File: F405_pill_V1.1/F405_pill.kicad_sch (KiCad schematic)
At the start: 42 parts, among them J1 Conn_01x04_Male, J2 Conn_01x04_Male, J4 TYPE-C-31-M-12, U1 STM32F405RGTx, U2 TCAN1051HDR, U3 LM1117-3.3, U4 STM32F405_pill, Y1 Crystal_GND24

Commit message: generated gerbers / BOMs
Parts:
- C3, C6: value 18p -> 12p; LCSC C92671 -> C1642
- D3: LCSC C87326 -> C90692
- R9: value 10k -> 20k; LCSC C269701 -> C365403
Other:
- note added: "Changes: power LED power LED resistor 18pF caps --> 12pF on xtal."
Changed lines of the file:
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@@
+    (effects (font (size 1.27 1.27)) (justify left bottom))
+  )
+  (text "Changes: \npower LED \npower LED resistor\n18pF caps --> 12pF on xtal."
+    (at 181.864 176.53 0)
     (effects (font (size 1.27 1.27)) (justify left bottom))
   )
@@
       (effects (font (size 1.27 1.27)) (justify left))
     )
-    (property "Value" "18p" (id 1) (at 46.99 74.9362 0)
+    (property "Value" "12p" (id 1) (at 46.99 74.9362 0)
       (effects (font (size 1.27 1.27)) (justify left))
     )
@@
       (effects (font (size 1.27 1.27)) hide)
     )
-    (property "LCSC" "C92671" (id 4) (at 44.45 73.66 0)
+    (property "LCSC" "C1642" (id 4) (at 44.45 73.66 0)
       (effects (font (size 1.27 1.27)) hide)
     )
@@
       (effects (font (size 1.27 1.27)) (justify left))
     )
-    (property "Value" "18p" (id 1) (at 24.13 74.93 0)
+    (property "Value" "12p" (id 1) (at 24.13 74.93 0)
       (effects (font (size 1.27 1.27)) (justify left))
     )
@@
       (effects (font (size 1.27 1.27)) hide)
     )
-    (property "LCSC" "C92671" (id 4) (at 29.845 73.66 0)
+    (property "LCSC" "C1642" (id 4) (at 29.845 73.66 0)
       (effects (font (size 1.27 1.27)) hide)
     )
@@
       (effects (font (size 1.27 1.27)) (justify right))
     )
-    (property "Value" "10k" (id 1) (at 270.51 64.77 0)
+    (property "Value" "20k" (id 1) (at 270.51 64.77 0)
       (effects (font (size 1.27 1.27)) (justify right))
     )
@@
       (effects (font (size 1.27 1.27)) hide)
     )
-    (property "LCSC" "C269701" (id 4) (at 267.97 62.23 0)
+    (property "LCSC" "C365403" (id 4) (at 267.97 62.23 0)
       (effects (font (size 1.27 1.27)) hide)
     )
@@
       (effects (font (size 1.27 1.27)) hide)
     )
-    (property "LCSC" "C87326" (id 6) (at 267.97 52.07 0)
+    (property "LCSC" "C90692" (id 6) (at 267.97 52.07 0)
       (effects (font (size 1.27 1.27)) hide)
     )
@@
     )
     (path "/6e59773b-20cf-43bf-aecf-380aa682d29d"
-      (reference "C3") (unit 1) (value "18p") (footprint "Capacitor_SMD:C_0603_1608Metric")
+      (reference "C3") (unit 1) (value "12p") (footprint "Capacitor_SMD:C_0603_1608Metric")
     )
     (path "/40c82e52-98e4-4cad-a0d7-023fceadffa0"
@@
     )
     (path "/1ec141c7-7133-40d6-b34a-de571f2b6dac"
-      (reference "C6") (unit 1) (value "18p") (footprint "Capacitor_SMD:C_0603_1608Metric")
+      (reference "C6") (unit 1) (value "12p") (footprint "Capacitor_SMD:C_0603_1608Metric")
     )
     (path "/ed8ad173-5f47-4e49-8771-8d0e48ed290e"
@@
     )
     (path "/ae295267-9bf4-4191-9631-7bb1dcc66970"
-      (reference "R9") (unit 1) (value "10k") (footprint "Resistor_SMD:R_0603_1608Metric")
+      (reference "R9") (unit 1) (value "20k") (footprint "Resistor_SMD:R_0603_1608Metric")
     )
     (path "/dba039c0-b01d-4dd9-be13-4d264a7c44db"

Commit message: new work
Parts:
- added C?: ??, Capacitor_SMD:C_0402_1005Metric, symbol Device:C_Small
- added R?: ??, Resistor_SMD:R_0603_1608Metric, symbol Device:R_Small
- added R?: 20k, Resistor_SMD:R_0603_1608Metric, symbol Device:R_Small
- R5: value 5k -> 20k; LCSC C365441 -> C365403
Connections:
- net GND: now also R?.1; no longer U2.5 (VIO)
- net USB_D+: no longer U4.29 (USB_D+)
- net USB_D-: no longer U4.28 (USB_D-)
- net at D2.1 (K), R5.2: no longer D1.1 (K)
- new net: D1.1 (K), R?.2
- new net DUAL1: U4.28 (DUAL1)
- new net DUAL2: U4.29 (DUAL2)
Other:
- note added: "ASSIGN PIN 5, VREF, TO WHAT?"
- note added: "A_OVERLIMIT LIN_A LIB_B LIB_C HIN_A HIN_B HIN_C V5V GND V3V3"
- note added: "Changes: Change caps on xtal from 18pF to 12pF Separate the two LEDs from the single resistor Remove ground from VIO pin on CAN RC between usb shell and pb12 to stop false trips"
- note added: "NC GND NC JP3 A_PHC_VSENSE JP2 A_PHB_VSENSE A_PHA_VSENSE A_SHC_AMP A_SHB_AMP A_SHA_AMP VSENSE A_THROTTLE JP3 HALL_C HALL_B HALL_A NC"
- note removed: "A_OVERLIMIT LIN_A LIB_B LIB_C HIN_A HIN_B HIN_C DUSB_DM DUSB_DP TIM2 CH1 TIM2 CH2 TIM3 CH1 TIM3 CH2 D_UART1_TX I2C1_SCL TIM4_CH1 D_UART1_RX I2C1_SDA TIM4_CH2 DI2C1_SCL TIM4_CH3 DI2C1_SDA TIM4_CH4 V5V GND V3V3"
- note removed: "Changes: power LED power LED resistor 18pF caps --> 12pF on xtal."
- note removed: "Fig 17 https://www.nxp.com/docs/en/supporting-information/AH1014.pdf"
- note removed: "NC GND NC PB10 D_GPIO PB2 D_GPIO JP3 A_PHC_VSENSE JP2 A_PHB_VSENSE A_PHA_VSENSE A_SHC_AMP A_SHB_AMP A_SHA_AMP VSENSE A_THROTTLE JP3 HALL_C HALL_B HALL_A NC"
- note removed: "TCAN1051HDR chip -- cheap at jlcpcb connect pin 3 to 5.0v pin 5 to 3.3v based on page 26 of the TCAN1051 data sheet"
- note removed: "https://easyeda.com/modules/ USB-C-Connector-circuit_245d3825d58f42648e08f3b1c22af371"
- moved on the sheet: C1, C10, C11, C12, C13, C14, C15, C16, C17, C18, C19, C2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

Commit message: new notes
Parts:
- added R12, R8: 1k, Resistor_SMD:R_0402_1005Metric, symbol Device:R_Small
- D3: footprint LED_SMD:LED_0603_1608Metric -> LED_SMD:LED_0402_1005Metric_Pad0.77x0.64mm_HandSolder
- R1, R2: footprint Resistor_SMD:R_0603_1608Metric -> Resistor_SMD:R_0402_1005Metric; LCSC C269701 -> (none)
- R10, R11: footprint Resistor_SMD:R_0603_1608Metric -> Resistor_SMD:R_0402_1005Metric; LCSC C365441 -> (none)
- R3, R4: footprint Resistor_SMD:R_0603_1608Metric -> Resistor_SMD:R_0402_1005Metric; LCSC C101133 -> (none)
- R5, R9: footprint Resistor_SMD:R_0603_1608Metric -> Resistor_SMD:R_0402_1005Metric; LCSC C365403 -> (none)
- R6: renamed from R?; footprint Resistor_SMD:R_0603_1608Metric -> Resistor_SMD:R_0402_1005Metric
- R7: renamed from R?; footprint Resistor_SMD:R_0603_1608Metric -> Resistor_SMD:R_0402_1005Metric; LCSC C365403 -> (none)
- gave numbers to parts that had none: 1
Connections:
- net PC4 is gone; now on net DUAL1: U1.24 (PC4)
- net PC5 is gone; now on net DUAL2: U1.25 (PC5)
- net DUAL1: now also R8.1
- net DUAL2: now also R12.1
- net PA5: now also U4.17 (PA5)
- net PB10: now also R8.2; no longer U4.34 (PB7)
- net PB11: now also R12.2; no longer U4.35 (PC10)
- net PB3: now also U4.30 (PB3); no longer U4.17 (PA5)
- net PB4: now also U4.31 (PB4); no longer U4.33 (PB6)
- net PB6: now also U4.33 (PB6); no longer U4.31 (PB4)
- net PB7: now also U4.34 (PB7); no longer U4.30 (PB3)
- net PB8: no longer U4.36 (PC11)
- net PB9: no longer U4.37 (PC12)
- net PC10: now also U4.35 (PC10)
- net PC11: now also U4.36 (PC11)
- net PC12: now also U4.37 (PC12)
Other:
- moved on the sheet: C17, C18, C19

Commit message: new text
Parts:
- C1: footprint Capacitor_SMD:C_0603_1608Metric -> Capacitor_SMD:C_0402_1005Metric; LCSC C19666 -> (none)
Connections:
- net PA15: now also D2.2 (A)
- net PC10: now also U4.37 (PC12); no longer U4.35 (PC10)
- net PC12: now also U4.35 (PC10); no longer D2.2 (A), U4.37 (PC12)
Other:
- note added: "Changes: Change caps on xtal from 18pF to 12pF Separate the two LEDs from the single resistor Remove ground from VIO pin on CAN RC between usb shell and pb12 to stop false trips PC12->PA15 to drive LED"
- note removed: "Changes: Change caps on xtal from 18pF to 12pF Separate the two LEDs from the single resistor Remove ground from VIO pin on CAN RC between usb shell and pb12 to stop false trips"
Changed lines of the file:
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@@
     (effects (font (size 1.27 1.27)) (justify left bottom))
   )
-  (text "Changes: \nChange caps on xtal from 18pF to 12pF\nSeparate the two LEDs from the single resistor\nRemove ground from VIO pin on CAN\nRC between usb shell and pb12 to stop false trips\n"
+  (text "Changes: \nChange caps on xtal from 18pF to 12pF\nSeparate the two LEDs from the single resistor\nRemove ground from VIO pin on CAN\nRC between usb shell and pb12 to stop false trips\nPC12->PA15 to drive LED\n"
     (at 152.908 167.894 0)
     (effects (font (size 1.27 1.27)) (justify left bottom))
@@
     )
   )
-  (global_label "PC12" (shape input) (at 151.003 71.755 180) (fields_autoplaced)
+  (global_label "PC10" (shape input) (at 151.003 71.755 180) (fields_autoplaced)
     (effects (font (size 1.27 1.27)) (justify right))
     (property "Intersheet References" "${INTERSHEET_REFS}" (id 0) (at 143.6309 71.6756 0)
@@
     )
   )
-  (global_label "PC10" (shape input) (at 151.003 66.675 180) (fields_autoplaced)
+  (global_label "PC12" (shape input) (at 151.003 66.675 180) (fields_autoplaced)
     (effects (font (size 1.27 1.27)) (justify right))
     (property "Intersheet References" "${INTERSHEET_REFS}" (id 0) (at 143.6309 66.5956 0)
@@
     )
   )
-  (global_label "PC12" (shape input) (at 225.171 39.878 90) (fields_autoplaced)
-    (effects (font (size 1.27 1.27)) (justify left))
-    (property "Intersheet References" "${INTERSHEET_REFS}" (id 0) (at 225.0916 32.5059 90)
+  (global_label "PA15" (shape input) (at 225.171 39.878 90) (fields_autoplaced)
+    (effects (font (size 1.27 1.27)) (justify left))
+    (property "Intersheet References" "${INTERSHEET_REFS}" (id 0) (at 225.0916 32.6873 90)
       (effects (font (size 1.27 1.27)) (justify left) hide)
     )
@@
       (effects (font (size 1.27 1.27)) (justify left))
     )
-    (property "Footprint" "Capacitor_SMD:C_0603_1608Metric" (id 2) (at 31.496 136.906 0)
+    (property "Footprint" "Capacitor_SMD:C_0402_1005Metric" (id 2) (at 31.496 136.906 0)
       (effects (font (size 1.27 1.27)) hide)
     )
@@
       (effects (font (size 1.27 1.27)) hide)
     )
-    (property "LCSC" "C19666" (id 6) (at 31.496 136.906 0)
+    (property "LCSC" "" (id 6) (at 31.496 136.906 0)
       (effects (font (size 1.27 1.27)) hide)
     )
@@
     )
     (path "/5adf4871-1582-4efa-95a7-6714120af869"
-      (reference "C1") (unit 1) (value "4u7") (footprint "Capacitor_SMD:C_0603_1608Metric")
+      (reference "C1") (unit 1) (value "4u7") (footprint "Capacitor_SMD:C_0402_1005Metric")
     )
     (path "/904cbc02-0482-486f-a7eb-64fd9657e60f"

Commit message: new high amp pic
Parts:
- added C22, C23: C_Polarized_Small, Capacitor_SMD:C_0603_1608Metric, symbol Device:C_Polarized_Small
- added U5: HT7550-1, Package_TO_SOT_SMD:SOT-89-3, symbol Regulator_Linear:L78L10_SOT89
- C1: LCSC (none) -> C315248
- C21: value ?? -> 10n; LCSC (none) -> C527024
- R1, R2: LCSC (none) -> C140214
- R10, R11: LCSC (none) -> C105872
- R12, R8: LCSC (none) -> C25543
- R3, R4: LCSC (none) -> C2960873
- R5, R7, R9: LCSC (none) -> C25765
- R6: value ?? -> 47 ohm; LCSC (none) -> C2909362
- U2: value TCAN1051HDR -> MAX3051EKA+T; footprint Package_SO:SOIC-8_3.9x4.9mm_P1.27mm -> Package_TO_SOT_SMD:SOT-23-8; LCSC C6952 -> C112005
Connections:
- net +5V: now also C23.1, U5.3 (IN); no longer U2.3 (VCC)
- net GND: now also C21.2, C22.2, C23.2, U5.2 (GND)
- net PB12: now also C21.1, R6.1; no longer U4.21 (PB12)
- net _PB12: now reaches R6.2
- net _PB12: now also U4.21 (PB12)
- new net VDO_I: C22.1, U2.3 (VCC), U5.1 (OUT)
- no-connect marks 4 -> 5
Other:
- note added: "CONFIRM: Does david want to use MAX3051 ?"
- note added: "Changes: Change caps on xtal from 18pF to 12pF Separate the two LEDs from the single resistor New CAN, with spike protection RC between GND and pb12 to stop false trips PC12->PA15 to drive LED"
- note added: "Overvoltage filter"
- note removed: "ASSIGN PIN 5, VREF, TO WHAT?"
- note removed: "Changes: Change caps on xtal from 18pF to 12pF Separate the two LEDs from the single resistor Remove ground from VIO pin on CAN RC between usb shell and pb12 to stop false trips PC12->PA15 to drive LED"
- moved on the sheet: C21, R6

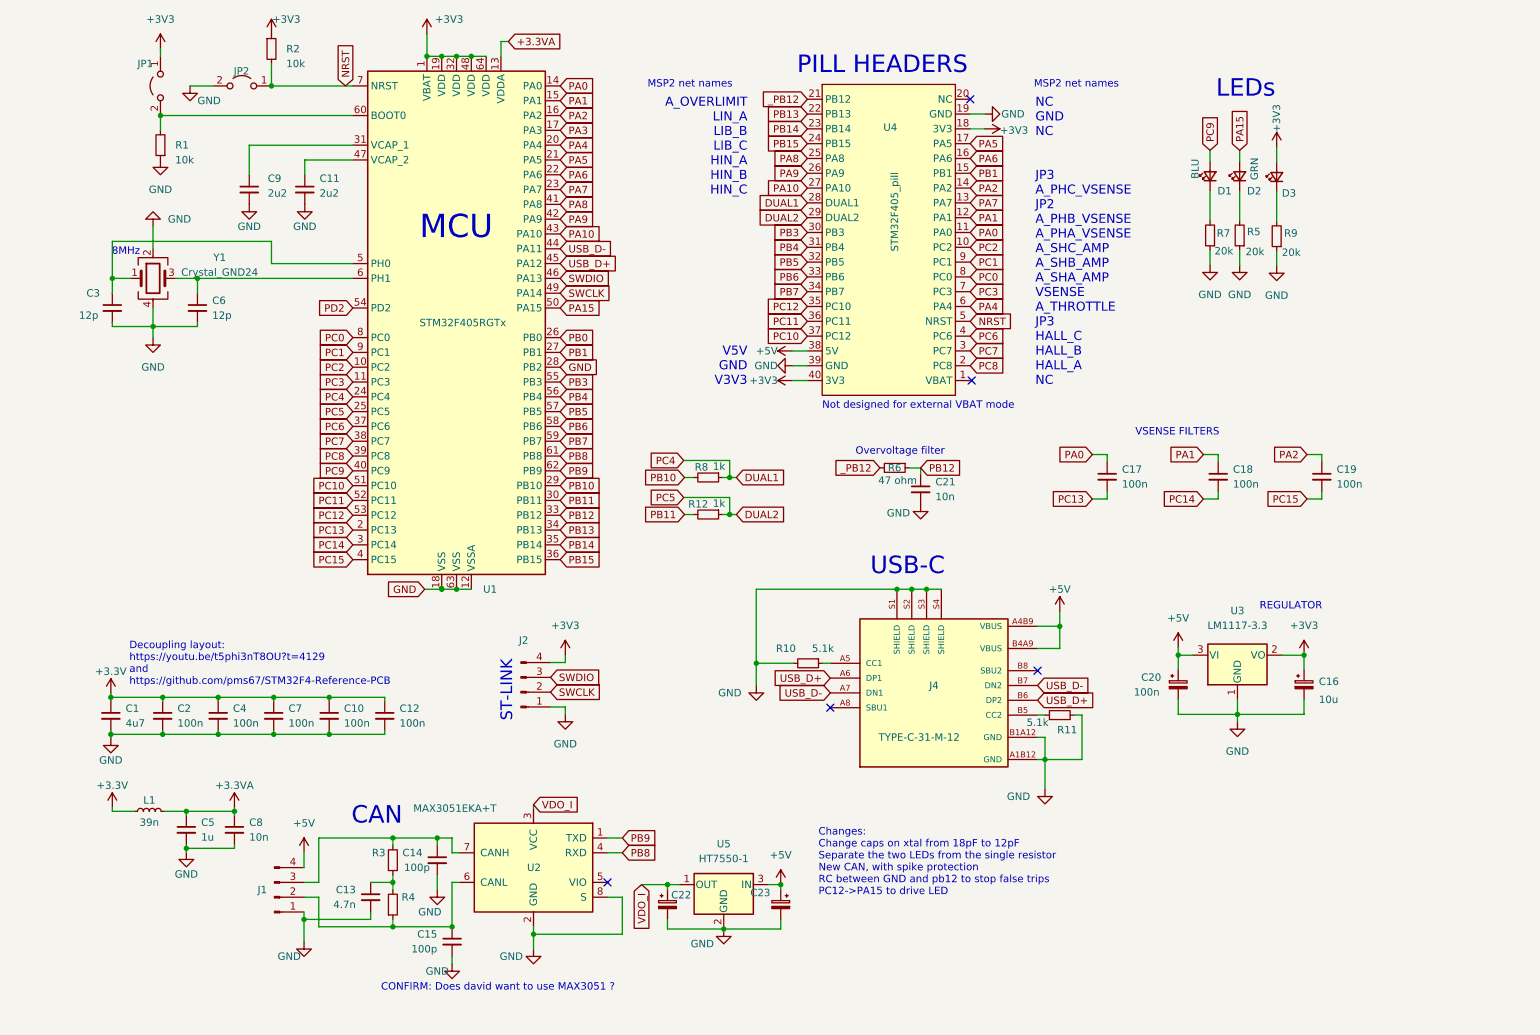
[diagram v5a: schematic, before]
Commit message: added a lot of LCSC#s
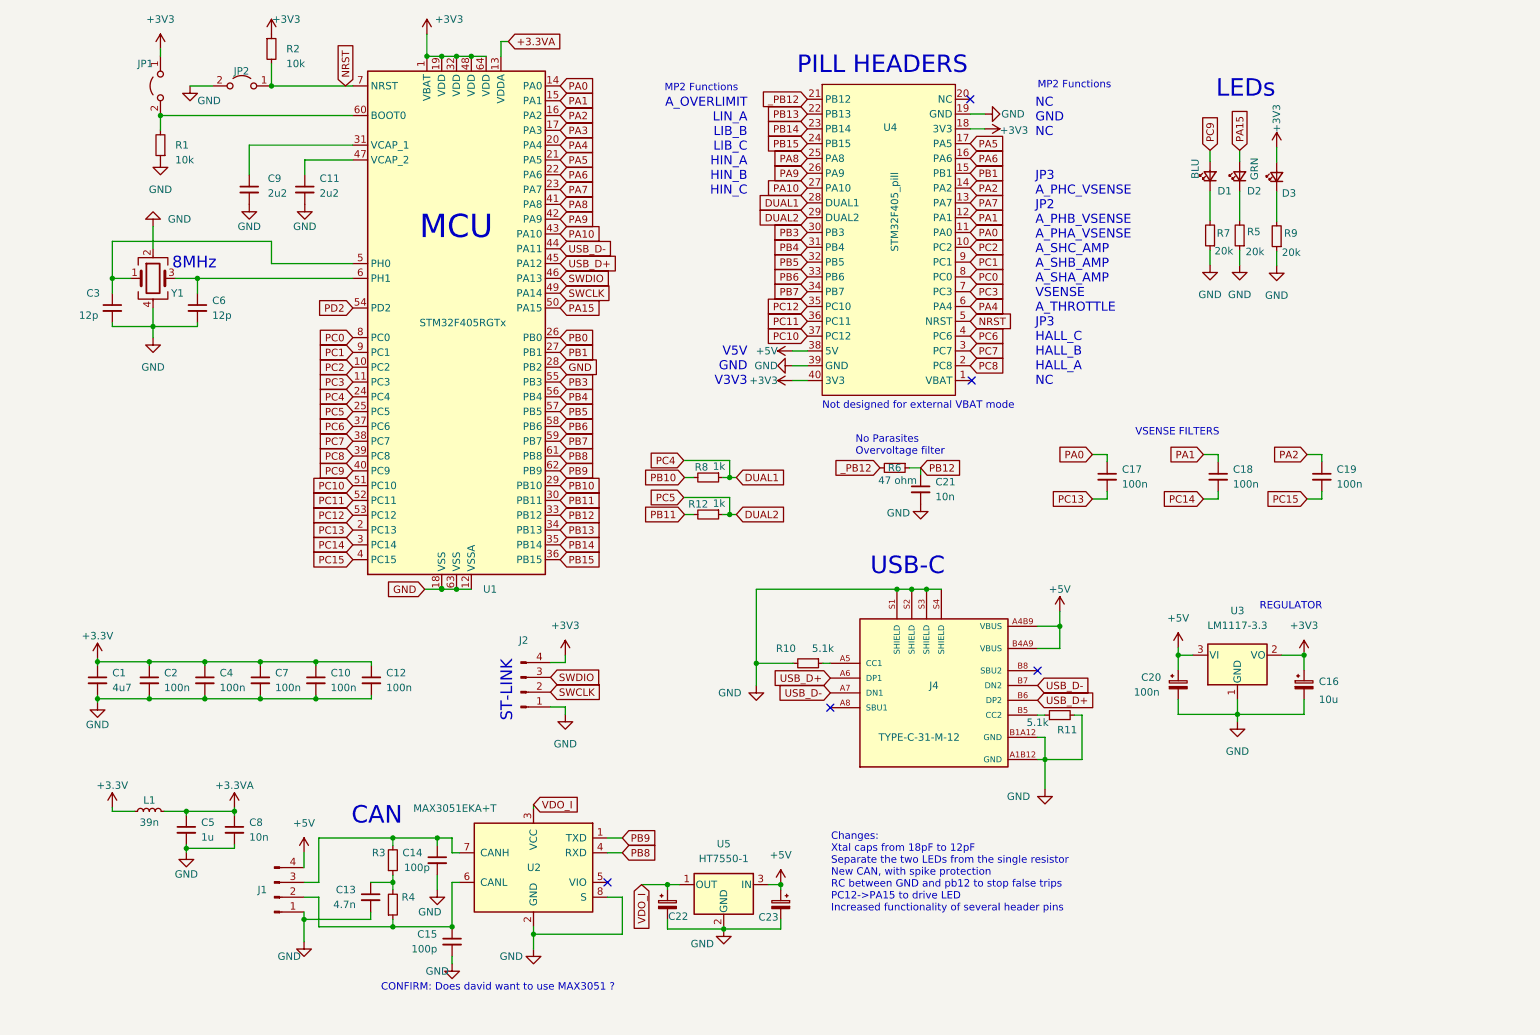
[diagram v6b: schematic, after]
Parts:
- C22, C23: LCSC (none) -> C962635
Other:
- note added: "Changes: Xtal caps from 18pF to 12pF Separate the two LEDs from the single resistor New CAN, with spike protection RC between GND and pb12 to stop false trips PC12->PA15 to drive LED Increased functionality of several header pins"
- note added: "MP2 Functions"
- note added: "No Parasites Overvoltage filter"
- note removed: "Changes: Change caps on xtal from 18pF to 12pF Separate the two LEDs from the single resistor New CAN, with spike protection RC between GND and pb12 to stop false trips PC12->PA15 to drive LED"
- note removed: "Decoupling layout: https://youtu.be/t5phi3nT8OU?t=4129 and https://github.com/pms67/STM32F4-Reference-PCB"
- note removed: "MSP2 net names"
- note removed: "Overvoltage filter"
- moved on the sheet: C1, C10, C12, C2, C4, C7

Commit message: finalizing
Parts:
- D3: value RED_LED -> RED
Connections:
- net at C14.1, J1.3 (Pin_3), R3.2: no longer U2.7 (CANH)
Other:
- note added: "A_OVERLIMIT LIN_A LIB_B LIB_C HIN_A HIN_B HIN_C TX3 SCL2 + ADC RX3 SDA2 + ADC SCK3 TX4 MISO3 TIM3 RX4 MOSI3, TIM3 CANRX TIM4 TX1 SCL1 CANTX RX1 SDA1 TIM4 SPI3 MOSI / GPIO SPI3 MISO RX4 SPI3 SCK TX4 V5V GND V3V3"
- note added: "BOARD REGULATOR"
- note added: "CAN REGULATOR"
- note added: "CONFIRM: correct wiring / values?"
- note added: "CONFIRM: correct wiring?"
- note added: "CONFIRM: ridiculously large LDO sized and wired correctly?"
- note added: "NC GND V3V3 ADC SPI1 DAC TIM2 ADC SPI1MISO TIM3 JP3 / FET TEMP A_PHC_VSENSE JP2 / MOTOR TEMP A_PHB_VSENSE A_PHA_VSENSE A_SHC_AMP A_SHB_AMP A_SHA_AMP VSENSE A_THROTTLE JP3 / FET TEMP HALL_C HALL_B HALL_A NC"
- note removed: "A_OVERLIMIT LIN_A LIB_B LIB_C HIN_A HIN_B HIN_C V5V GND V3V3"
- note removed: "NC GND NC JP3 A_PHC_VSENSE JP2 A_PHB_VSENSE A_PHA_VSENSE A_SHC_AMP A_SHB_AMP A_SHA_AMP VSENSE A_THROTTLE JP3 HALL_C HALL_B HALL_A NC"
- note removed: "REGULATOR"
- moved on the sheet: C1, C10, C12, C13, C14, C15, C16, C17, C18, C19, C2, C20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
